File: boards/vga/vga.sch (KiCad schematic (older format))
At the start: 84 parts, among them J1 Conn_02x20_Odd_Even, J2 L77HDE15SD1CH4RHNVGA, Q1 BSS84AK, U1 SN74LV161APW, U10 62256-TSOP, U11 SN74LV161APW, U12 SN74LV161APW, U13 SN74LV244APW, U14 SN74LV20APW, U15 74LV32APWJ, U16 74LV08APWJ, U17 AT28C256-PLCC32, U18 SN74LV273APW, U19 SN74LV273APW, U2 SN74LV161APW, U20 CD74AC151M96, U21 SN74LV157APW, U22 SN74LV10APW, U23 SN74LV74APW, U24 SN74LV00APW, U25 74LV32APWJ, U26 SN74LV21APW, U27 SN74AHC1G86DBVR, U28 74LV32APWJ, U29 74LV08APWJ, U3 SN74LV157APW, U30 SN74LV74APW, U4 SN74LV157APW, U5 SN74LV157APW, U6 SN74LV161APW, U7 SN74LV161APW, U8 SN74LV244APW, U9 62256-TSOP, X1 MXO45HS-3C-25M1750

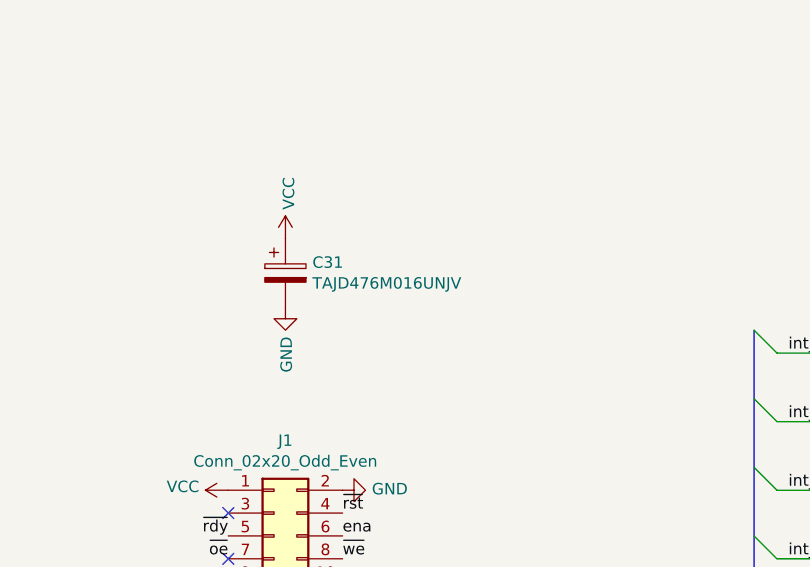
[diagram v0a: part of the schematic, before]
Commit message: VGA board: change capacitor footprint
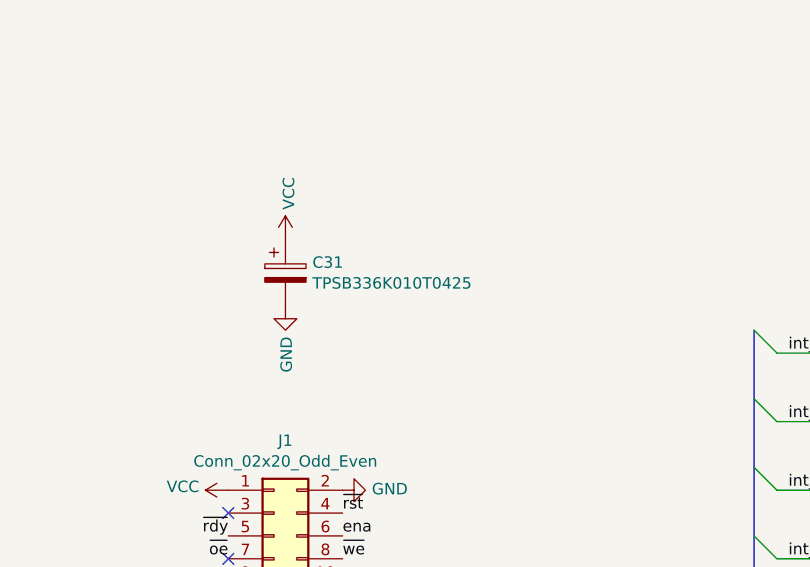
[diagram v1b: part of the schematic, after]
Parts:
- C31: value TAJD476M016UNJV -> TPSB336K010T0425; footprint Capacitor_Tantalum_SMD:CP_EIA-7343-40_Kemet-Y -> Capacitor_Tantalum_SMD:CP_EIA-3528-15_AVX-H_Pad1.50x2.35mm_HandSolder
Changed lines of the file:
@@
 P 1800 4200
 F 0 "C31" H 1918 4246 50  0000 L CNN
-F 1 "TAJD476M016UNJV" H 1918 4155 50  0000 L CNN
-F 2 "Capacitor_Tantalum_SMD:CP_EIA-7343-40_Kemet-Y" H 1838 4050 50  0001 C CNN
+F 1 "TPSB336K010T0425" H 1918 4155 50  0000 L CNN
+F 2 "Capacitor_Tantalum_SMD:CP_EIA-3528-15_AVX-H_Pad1.50x2.35mm_HandSolder" H 1838 4050 50  0001 C CNN
 F 3 "~" H 1800 4200 50  0001 C CNN
 	1    1800 4200
@@
 	0    -1   -1   0
 $EndComp
+$Comp
+L Device:R R6
+U 1 1 60AFB465
+P 4350 13550
+F 0 "R6" V 4550 13450 50  0000 C CNN
+F 1 "50" V 4450 13450 50  0000 C CNN
+F 2 "Resistor_SMD:R_0805_2012Metric" V 4280 13550 50  0001 C CNN
+F 3 "~" H 4350 13550 50  0001 C CNN
+	1    4350 13550
+	0    -1   -1   0
+$EndComp
 Wire Bus Line
 	11050 5150 11050 5850
@@
 Wire Bus Line
 	6050 4500 6050 10250
-$Comp
-L Device:R R6
-U 1 1 60AFB465
-P 4350 13550
-F 0 "R6" V 4550 13450 50  0000 C CNN
-F 1 "50" V 4450 13450 50  0000 C CNN
-F 2 "Resistor_SMD:R_0805_2012Metric" V 4280 13550 50  0001 C CNN
-F 3 "~" H 4350 13550 50  0001 C CNN
-	1    4350 13550
-	0    -1   -1   0
-$EndComp
 $EndSCHEMATC

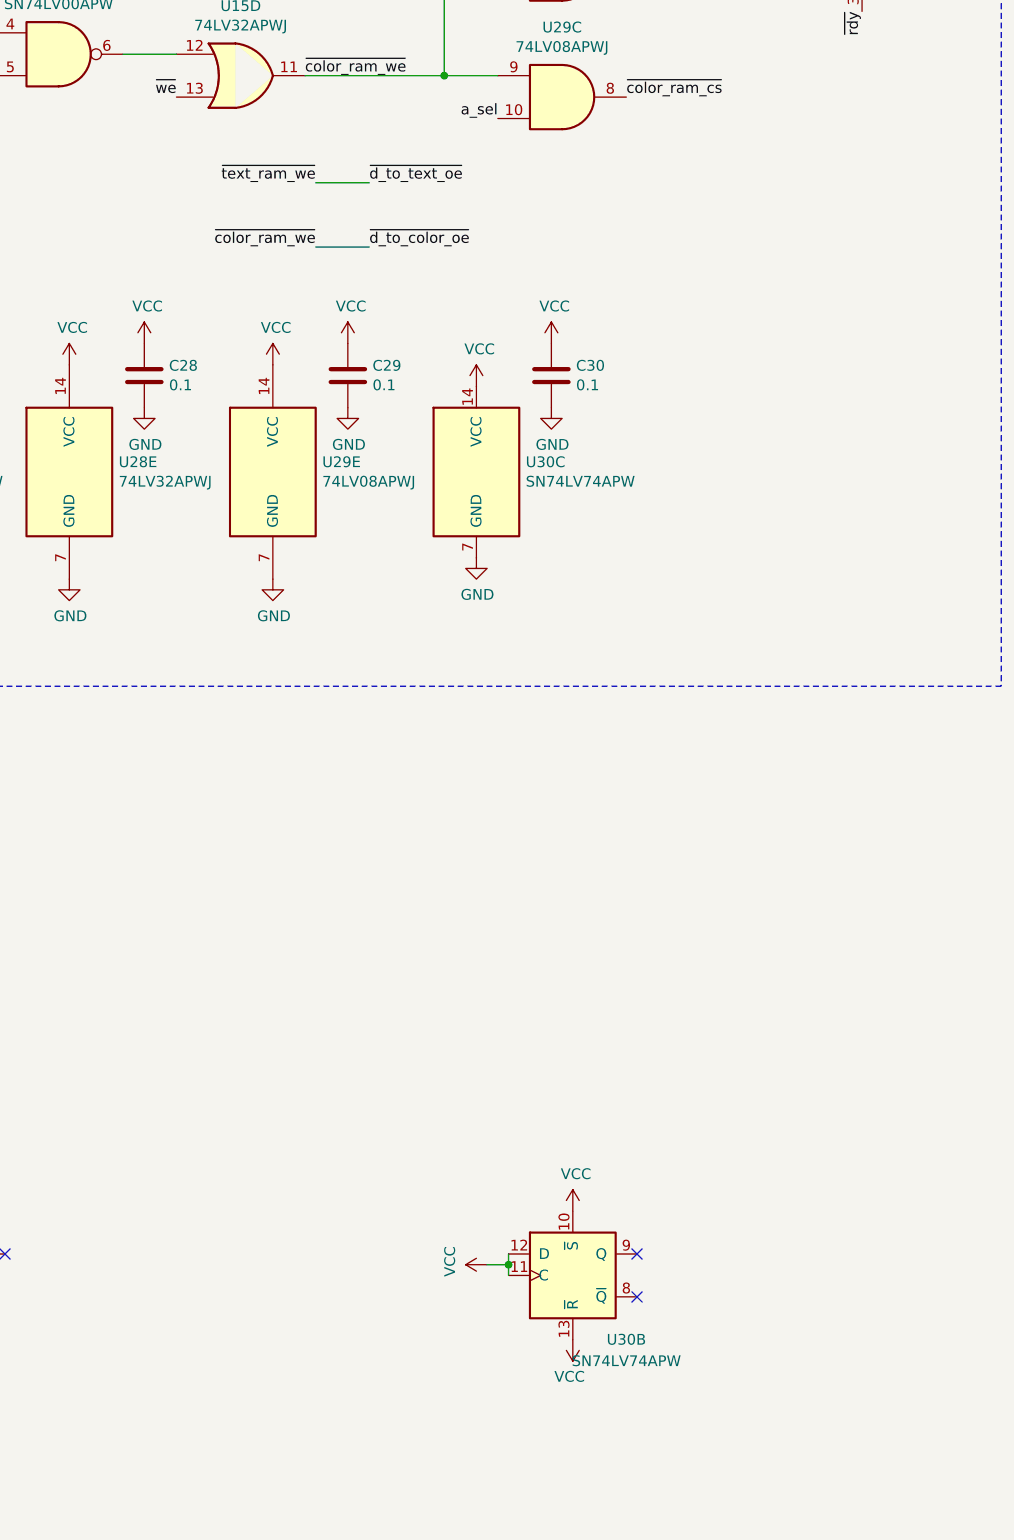
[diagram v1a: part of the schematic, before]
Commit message: VGA: never leave internal busses in high-z state
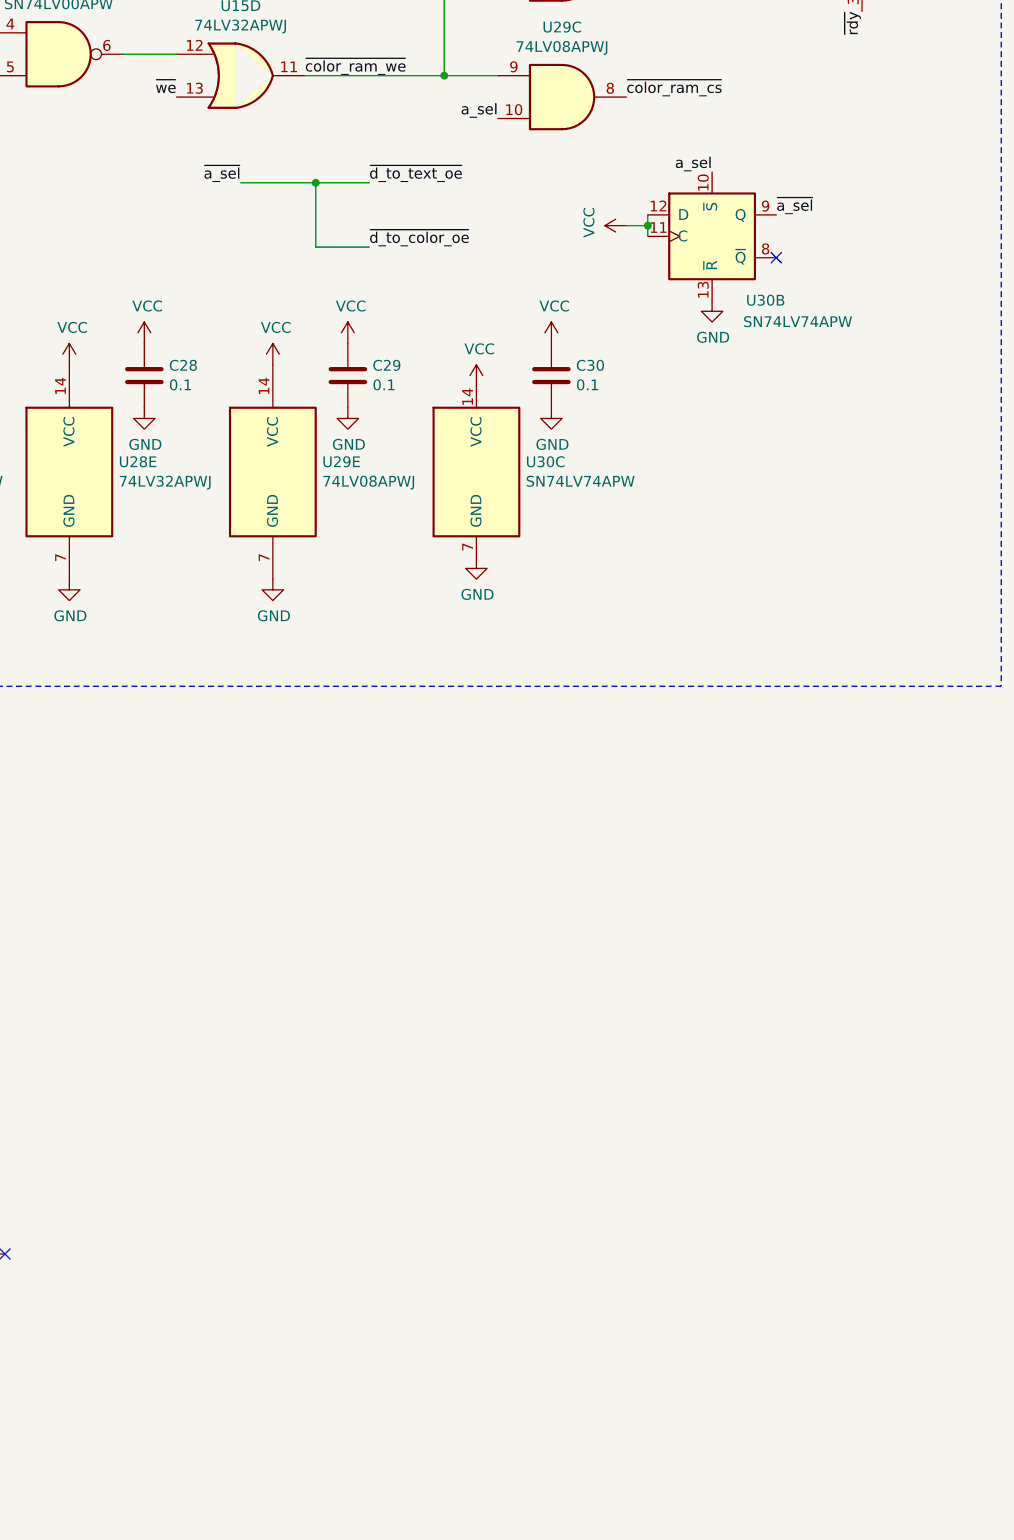
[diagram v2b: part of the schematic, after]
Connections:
- net GND: now also U30.13 (~R)
- net VCC: no longer U30.10 (~S), U30.13 (~R)
- net a_sel: now also U30.10 (~S)
- net ~color_ram_we: no longer U13.1 (1OE), U13.19 (2OE)
- net ~a_sel: now reaches U30.9 (Q)
- net ~a_sel: now also U13.1 (1OE), U13.19 (2OE), U8.1 (1OE), U8.19 (2OE)
- net ~d_to_text_oe renamed ~text_ram_we
- net ~text_ram_we: no longer U8.1 (1OE), U8.19 (2OE)
- no-connect marks 27 -> 26
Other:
- moved on the sheet: U30B
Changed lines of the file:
@@
-$Comp
-L 74xx:74LS74 U30
-U 2 1 5FE477DE
-P 20550 19900
-F 0 "U30" H 20800 19600 50  0000 C CNN
-F 1 "SN74LV74APW" H 20800 19500 50  0000 C CNN
-F 2 "Package_SO:TSSOP-14_4.4x5mm_P0.65mm" H 20550 19900 50  0001 C CNN
-F 3 "https://www.ti.com/lit/ds/symlink/sn74lv74a.pdf" H 20550 19900 50  0001 C CNN
-	2    20550 19900
-	1    0    0    -1
-$EndComp
 $Comp
 L 74xx:74LS74 U30
@@
 NoConn ~ 17900 19800
 NoConn ~ 16700 19800
-NoConn ~ 20850 20000
-NoConn ~ 20850 19800
-$Comp
-L power:VCC #PWR0165
-U 1 1 60251D4C
-P 20550 20200
-F 0 "#PWR0165" H 20550 20050 50  0001 C CNN
-F 1 "VCC" H 20565 20373 50  0000 C CNN
-F 2 "" H 20550 20200 50  0001 C CNN
-F 3 "" H 20550 20200 50  0001 C CNN
-	1    20550 20200
-	-1   0    0    1
-$EndComp
-$Comp
-L power:VCC #PWR0164
-U 1 1 6025314A
-P 20550 19600
-F 0 "#PWR0164" H 20550 19450 50  0001 C CNN
-F 1 "VCC" H 20565 19773 50  0000 C CNN
-F 2 "" H 20550 19600 50  0001 C CNN
-F 3 "" H 20550 19600 50  0001 C CNN
-	1    20550 19600
-	1    0    0    -1
-$EndComp
-$Comp
-L power:VCC #PWR0161
-U 1 1 6025389C
-P 20150 19850
-F 0 "#PWR0161" H 20150 19700 50  0001 C CNN
-F 1 "VCC" H 20165 20023 50  0000 C CNN
-F 2 "" H 20150 19850 50  0001 C CNN
-F 3 "" H 20150 19850 50  0001 C CNN
-	1    20150 19850
-	0    -1   -1   0
-$EndComp
-Wire Wire Line
-	20250 19800 20250 19850
-Wire Wire Line
-	20150 19850 20250 19850
-Connection ~ 20250 19850
-Wire Wire Line
-	20250 19850 20250 19900
 $Comp
 L power:VCC #PWR0137
@@
 Text Label 19600 15100 0    50   ~ 0
 ~d_to_color_oe
-Text Label 19350 14800 2    50   ~ 0
-~text_ram_we
-Text Label 19350 15100 2    50   ~ 0
-~color_ram_we
 Wire Wire Line
 	19350 14800 19600 14800
@@
 	0    -1   -1   0
 $EndComp
+Wire Wire Line
+	20900 15000 20900 15050
+Connection ~ 20900 15000
+Wire Wire Line
+	20800 15000 20900 15000
+Wire Wire Line
+	20900 14950 20900 15000
+$Comp
+L power:VCC #PWR0161
+U 1 1 6025389C
+P 20800 15000
+F 0 "#PWR0161" H 20800 14850 50  0001 C CNN
+F 1 "VCC" H 20815 15173 50  0000 C CNN
+F 2 "" H 20800 15000 50  0001 C CNN
+F 3 "" H 20800 15000 50  0001 C CNN
+	1    20800 15000
+	0    -1   -1   0
+$EndComp
+NoConn ~ 21500 15150
+$Comp
+L 74xx:74LS74 U30
+U 2 1 5FE477DE
+P 21200 15050
+F 0 "U30" H 21450 14750 50  0000 C CNN
+F 1 "SN74LV74APW" H 21600 14650 50  0000 C CNN
+F 2 "Package_SO:TSSOP-14_4.4x5mm_P0.65mm" H 21200 15050 50  0001 C CNN
+F 3 "https://www.ti.com/lit/ds/symlink/sn74lv74a.pdf" H 21200 15050 50  0001 C CNN
+	2    21200 15050
+	1    0    0    -1
+$EndComp
+Text Label 21500 14950 0    50   ~ 0
+~a_sel
+$Comp
+L power:GND #PWR?
+U 1 1 5FE54E72
+P 21200 15350
+F 0 "#PWR?" H 21200 15100 50  0001 C CNN
+F 1 "GND" H 21205 15177 50  0000 C CNN
+F 2 "" H 21200 15350 50  0001 C CNN
+F 3 "" H 21200 15350 50  0001 C CNN
+	1    21200 15350
+	1    0    0    -1
+$EndComp
+Text Label 21200 14750 2    50   ~ 0
+a_sel
+Wire Wire Line
+	19000 14800 19350 14800
+Wire Wire Line
+	19350 14800 19350 15100
 Wire Bus Line
 	11050 5150 11050 5850
@@
 Wire Bus Line
 	6050 4500 6050 10250
+Connection ~ 19350 14800
+Text Label 19000 14800 2    50   ~ 0
+~a_sel
 $EndSCHEMATC
